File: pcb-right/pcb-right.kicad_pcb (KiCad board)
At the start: 2 copper layers, 124.8 x 104.5 mm, 43 parts, among them J2 BAT, U2 xiao-ble

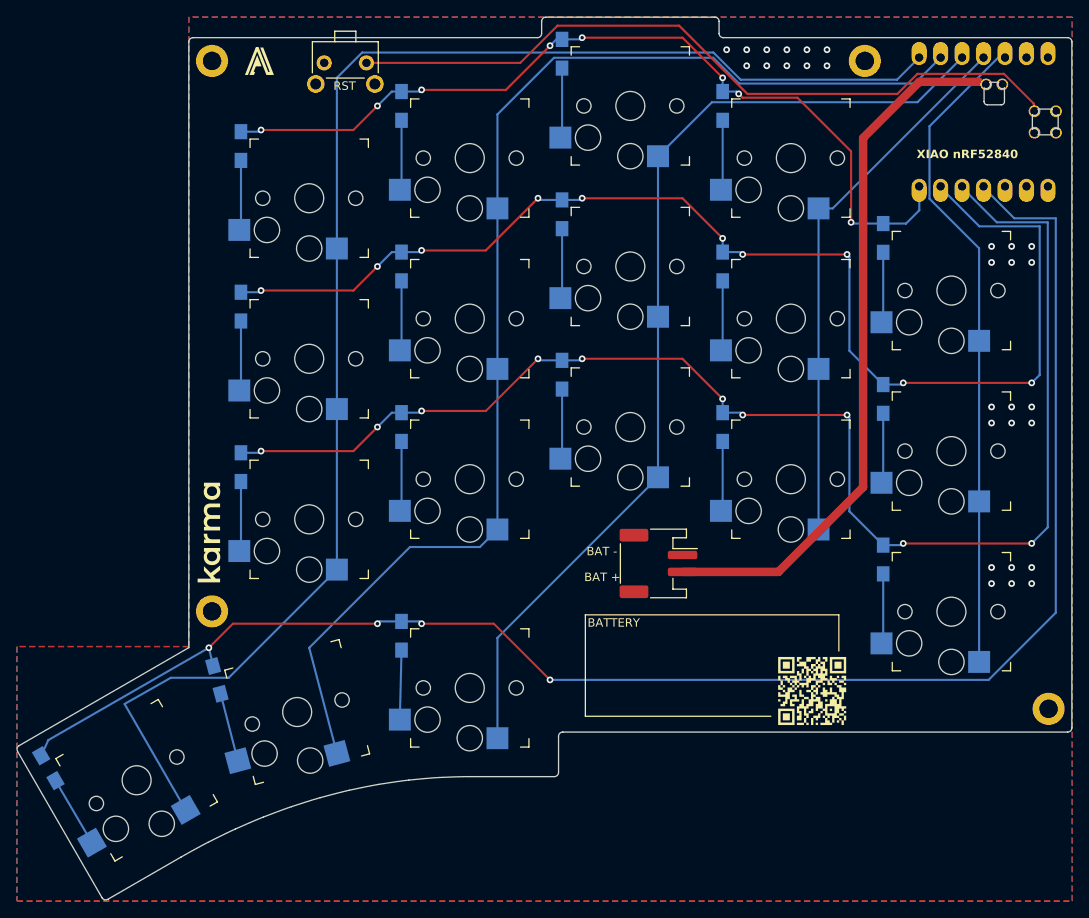
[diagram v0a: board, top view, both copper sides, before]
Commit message: support kailh choc v2
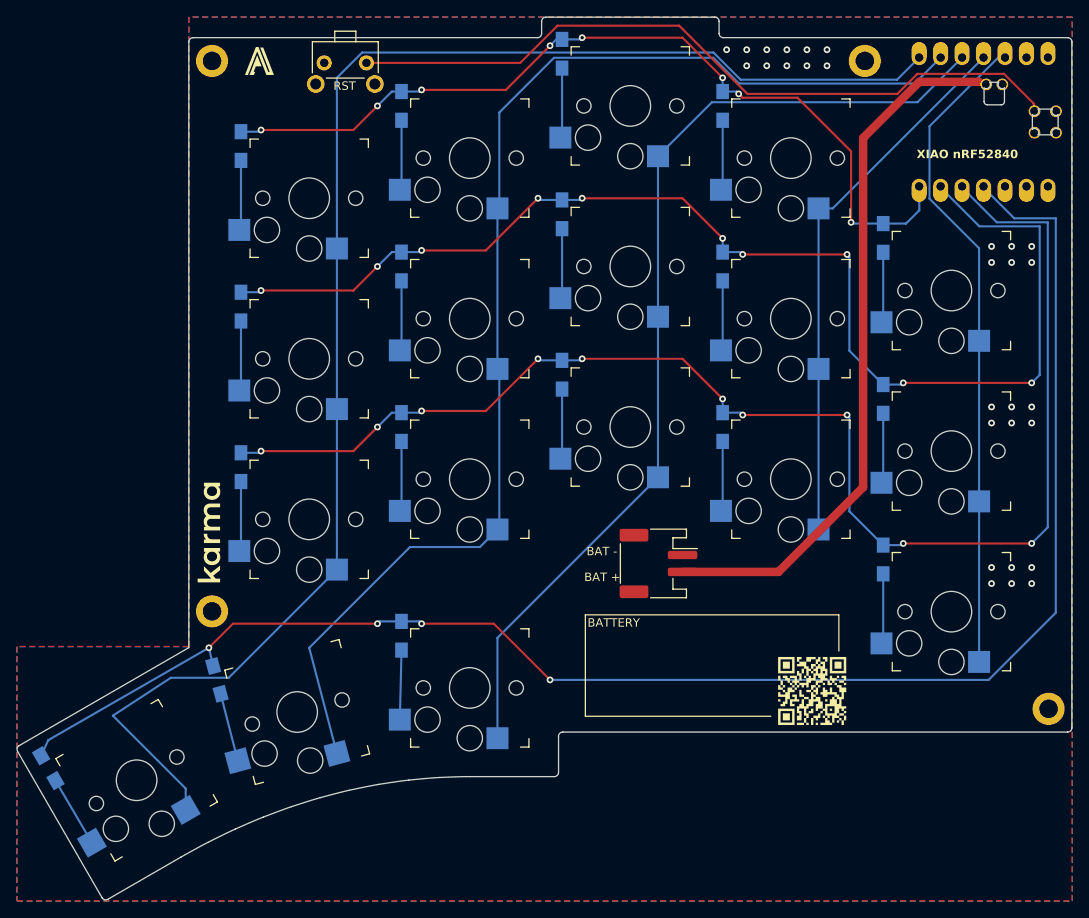
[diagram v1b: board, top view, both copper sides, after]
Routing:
- net COL4_R: track 176.5 -> 178.6 mm
